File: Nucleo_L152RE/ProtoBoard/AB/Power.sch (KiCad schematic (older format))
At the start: 52 parts, among them J1 EXTPower, P10 GND, P11 GND, P12 GND, P13 GND, P14 GND, P15 GND, P16 GND, P17 GND, P18 GND, P19 3.3Ctl, P20 3.3Ctl, P21 3.3Ctl, P22 3.3V, P23 3.3V, P24 3.3V, P25 5.0V, P26 5.0V, P27 5.0V, P28 Servo, P29 Servo, P30 Servo, P31 Power2, P33 VinPower, P34 ServoPower, P35 Power1, P7 GND, P8 GND, P9 GND, U1 LDS3985

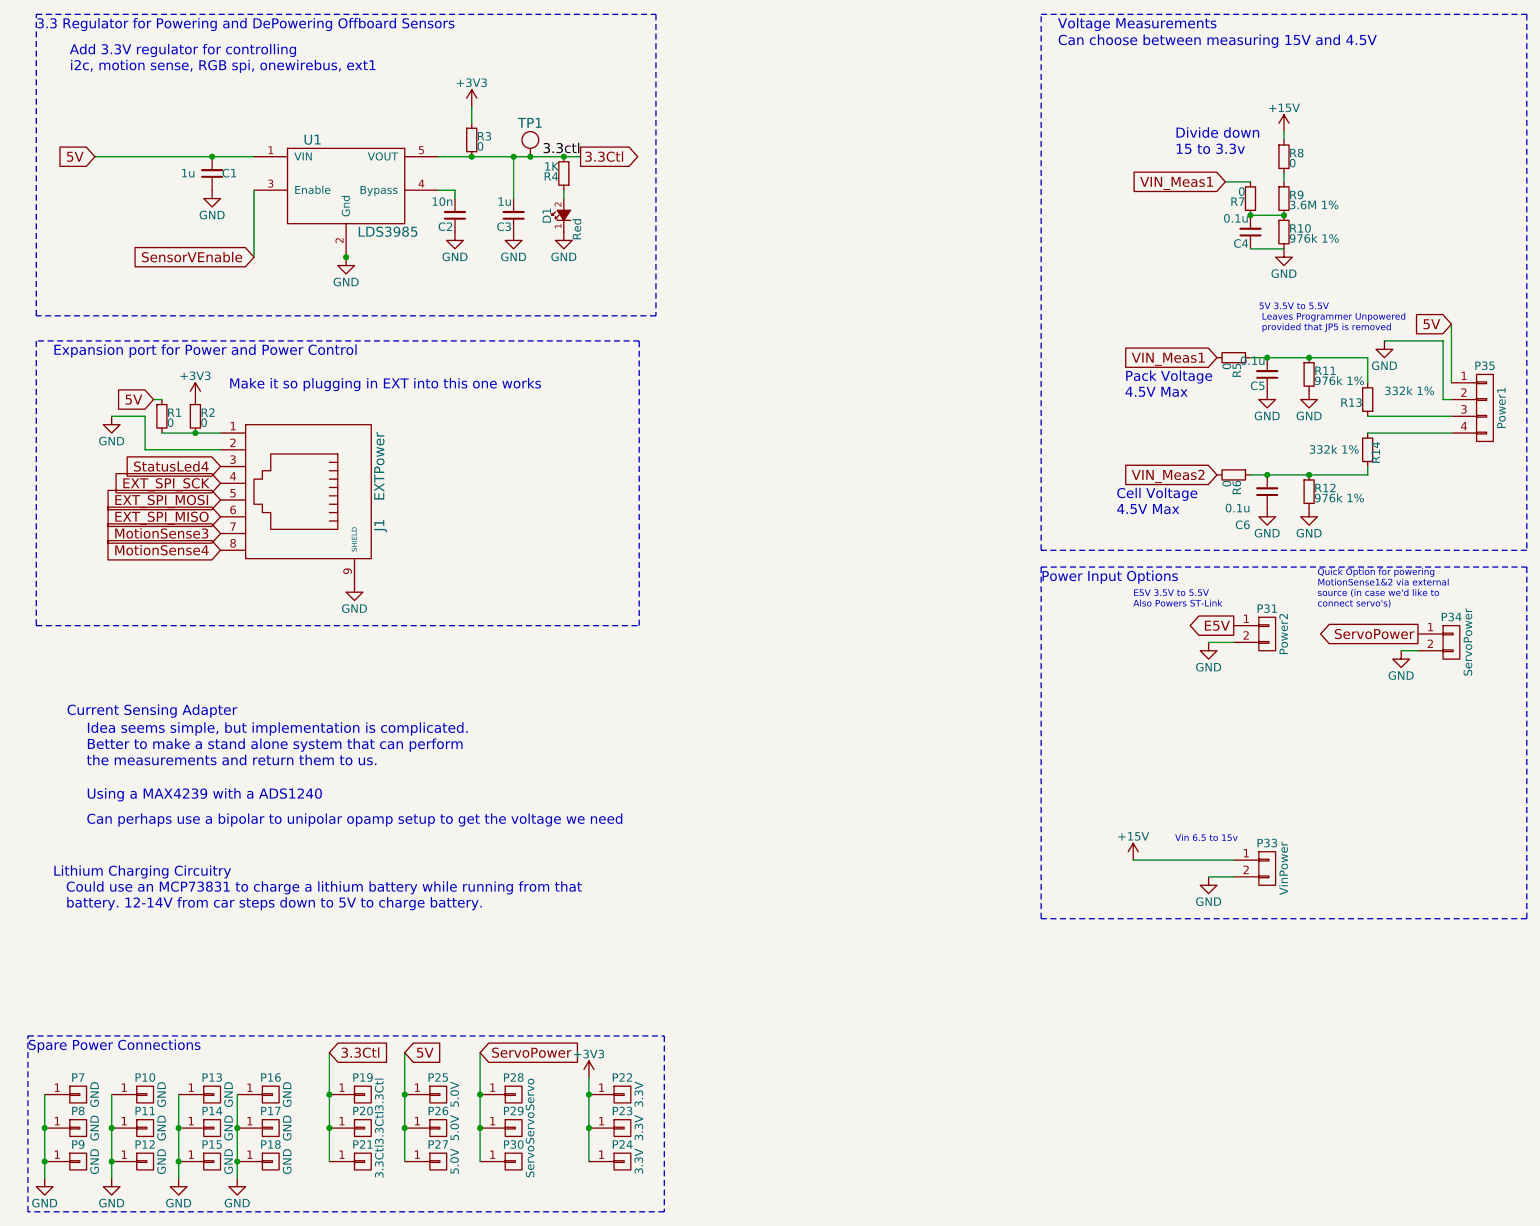
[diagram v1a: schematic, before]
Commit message: Final draft with all traces and artwork in place.
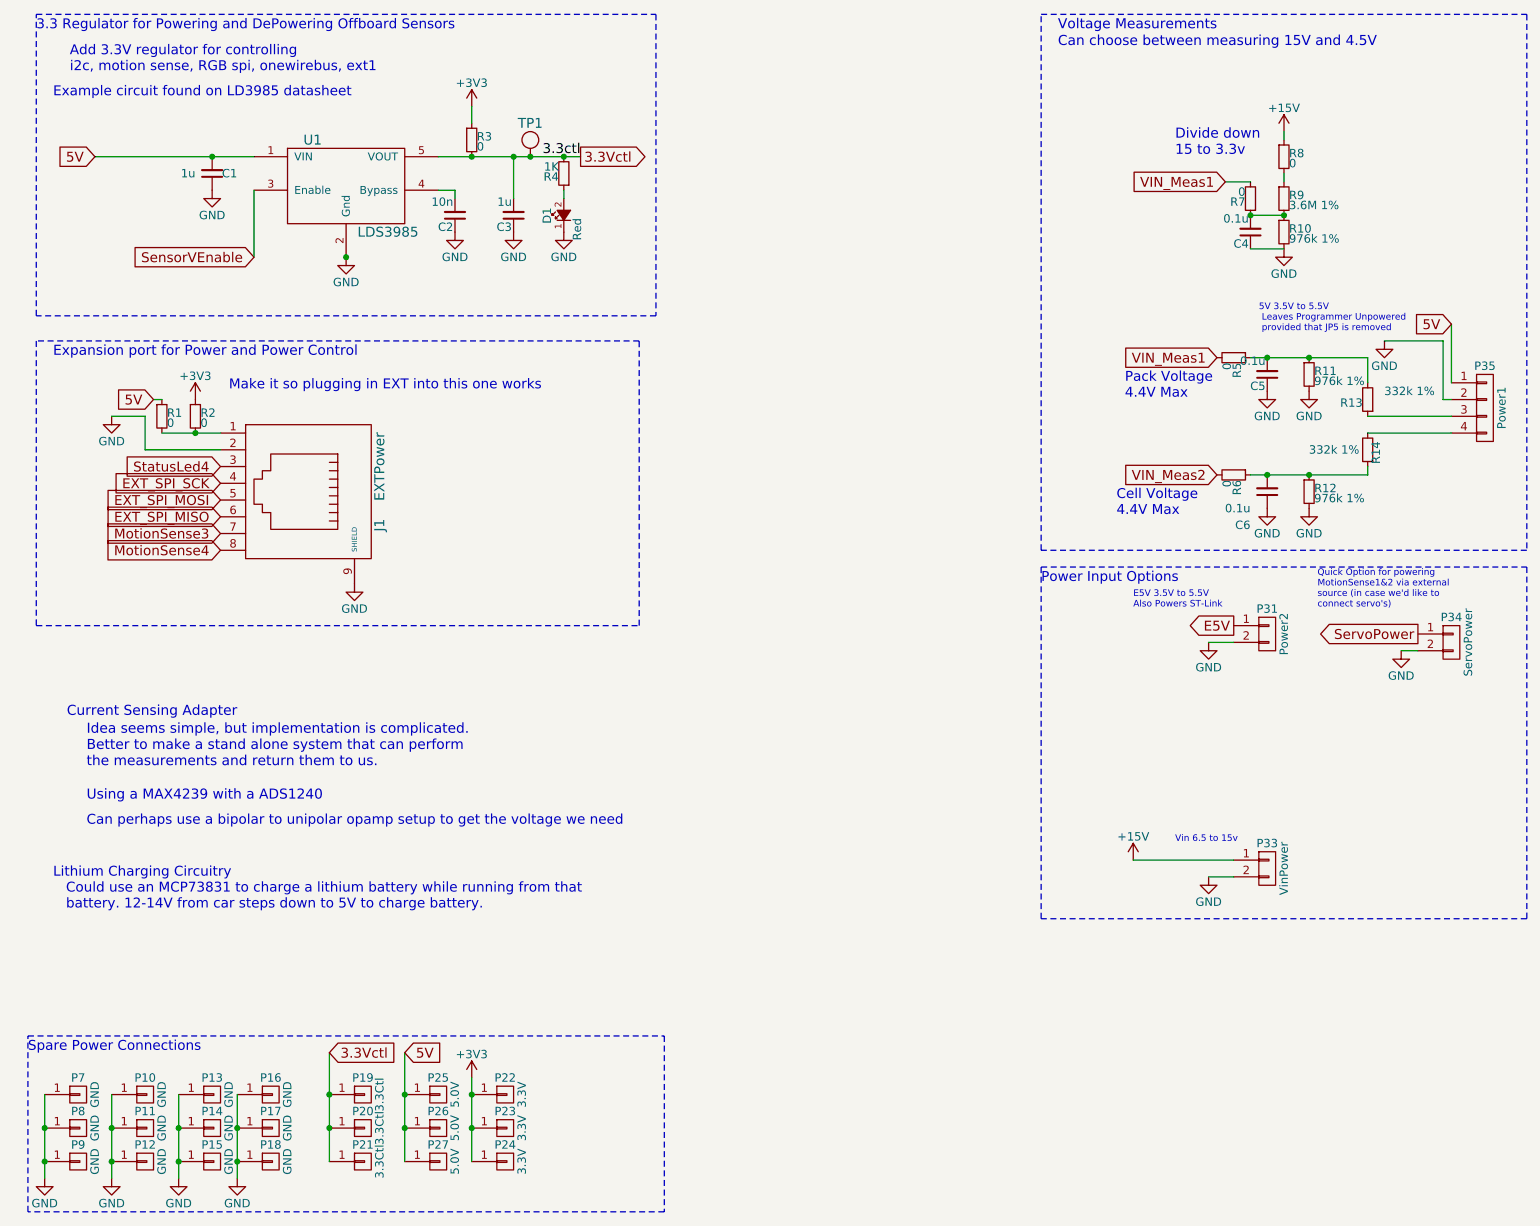
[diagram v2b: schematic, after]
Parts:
- removed P28, P29, P30: Servo, Pin_Headers:Pin_Header_Straight_1x01, symbol CONN_01X01
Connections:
- net 3.3Ctl renamed 3.3Vctl
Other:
- note added: "Cell Voltage\n4.4V Max"
- note added: "Example circuit found on LD3985 datasheet"
- note added: "Pack Voltage\n4.4V Max"
- note removed: "Cell Voltage\n4.5V Max"
- note removed: "Pack Voltage\n4.5V Max"
- moved on the sheet: P22, P23, P24
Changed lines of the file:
@@
 Sheet 2 5
 Title "Expansion Board For STM32 Nucleo-L152RE"
-Date "Saturday, May 23, 2015"
-Rev "AB - Draft"
+Date "Sunday, May 31, 2015"
+Rev "AB - Final Draft"
 Comp "Open Source Hardware"
 Comment1 "MIT License"
@@
 $EndComp
 $Comp
-L GND #PWR04
+L GND #PWR03
 U 1 1 555A6ADF
 P 2550 2100
-F 0 "#PWR04" H 2550 1850 50  0001 C CNN
+F 0 "#PWR03" H 2550 1850 50  0001 C CNN
 F 1 "GND" H 2550 1950 50  0000 C CNN
 F 2 "" H 2550 2100 60  0000 C CNN
@@
 $EndComp
 $Comp
-L GND #PWR05
+L GND #PWR04
 U 1 1 555A6AE5
 P 3200 1950
-F 0 "#PWR05" H 3200 1700 50  0001 C CNN
+F 0 "#PWR04" H 3200 1700 50  0001 C CNN
 F 1 "GND" H 3200 1800 50  0000 C CNN
 F 2 "" H 3200 1950 60  0000 C CNN
@@
 $EndComp
 $Comp
-L GND #PWR06
+L GND #PWR05
 U 1 1 555A6AEB
 P 3550 1950
-F 0 "#PWR06" H 3550 1700 50  0001 C CNN
+F 0 "#PWR05" H 3550 1700 50  0001 C CNN
 F 1 "GND" H 3550 1800 50  0000 C CNN
 F 2 "" H 3550 1950 60  0000 C CNN
@@
 $EndComp
 $Comp
-L GND #PWR07
+L GND #PWR06
 U 1 1 555A6AF1
 P 1750 1700
-F 0 "#PWR07" H 1750 1450 50  0001 C CNN
+F 0 "#PWR06" H 1750 1450 50  0001 C CNN
 F 1 "GND" H 1750 1550 50  0000 C CNN
 F 2 "" H 1750 1700 60  0000 C CNN
@@
 Voltage Measurements\n
 $Comp
-L GND #PWR08
+L GND #PWR07
 U 1 1 555A784D
 P 8150 2050
-F 0 "#PWR08" H 8150 1800 50  0001 C CNN
+F 0 "#PWR07" H 8150 1800 50  0001 C CNN
 F 1 "GND" H 8150 1900 50  0000 C CNN
 F 2 "" H 8150 2050 60  0000 C CNN
@@
 $EndComp
 $Comp
-L GND #PWR09
+L GND #PWR08
 U 1 1 555A7864
 P 7700 4400
-F 0 "#PWR09" H 7700 4150 50  0001 C CNN
+F 0 "#PWR08" H 7700 4150 50  0001 C CNN
 F 1 "GND" H 7700 4250 50  0000 C CNN
 F 2 "" H 7700 4400 60  0000 C CNN
@@
 $EndComp
 $Comp
-L GND #PWR010
+L GND #PWR09
 U 1 1 555A786A
 P 7700 5800
-F 0 "#PWR010" H 7700 5550 50  0001 C CNN
+F 0 "#PWR09" H 7700 5550 50  0001 C CNN
 F 1 "GND" H 7700 5650 50  0000 C CNN
 F 2 "" H 7700 5800 60  0000 C CNN
@@
 $EndComp
 $Comp
-L GND #PWR011
+L GND #PWR010
 U 1 1 555A787C
 P 2600 4050
-F 0 "#PWR011" H 2600 3800 50  0001 C CNN
+F 0 "#PWR010" H 2600 3800 50  0001 C CNN
 F 1 "GND" H 2600 3900 50  0000 C CNN
 F 2 "" H 2600 4050 60  0000 C CNN
@@
 $EndComp
 $Comp
-L GND #PWR012
+L GND #PWR011
 U 1 1 555A7885
 P 1150 3050
-F 0 "#PWR012" H 1150 2800 50  0001 C CNN
+F 0 "#PWR011" H 1150 2800 50  0001 C CNN
 F 1 "GND" H 1150 2900 50  0000 C CNN
 F 2 "" H 1150 3050 60  0000 C CNN
@@
 Expansion port for Power and Power Control\n
 $Comp
-L +15V #PWR013
+L +15V #PWR012
 U 1 1 555A788E
 P 7250 5700
-F 0 "#PWR013" H 7250 5550 50  0001 C CNN
+F 0 "#PWR012" H 7250 5550 50  0001 C CNN
 F 1 "+15V" H 7250 5840 50  0000 C CNN
 F 2 "" H 7250 5700 60  0000 C CNN
@@
 $EndComp
 $Comp
-L +15V #PWR014
+L +15V #PWR013
 U 1 1 555A7894
 P 8150 1350
-F 0 "#PWR014" H 8150 1200 50  0001 C CNN
+F 0 "#PWR013" H 8150 1200 50  0001 C CNN
 F 1 "+15V" H 8150 1490 50  0000 C CNN
 F 2 "" H 8150 1350 60  0000 C CNN
@@
 	1350 3050 1150 3050
 $Comp
-L +3V3 #PWR015
+L +3V3 #PWR014
 U 1 1 555A78D8
 P 1650 2950
-F 0 "#PWR015" H 1650 2800 50  0001 C CNN
+F 0 "#PWR014" H 1650 2800 50  0001 C CNN
 F 1 "+3V3" H 1650 3090 50  0000 C CNN
 F 2 "" H 1650 2950 60  0000 C CNN
@@
 $EndComp
 $Comp
-L GND #PWR016
+L GND #PWR015
 U 1 1 555A7927
 P 8750 2600
-F 0 "#PWR016" H 8750 2350 50  0001 C CNN
+F 0 "#PWR015" H 8750 2350 50  0001 C CNN
 F 1 "GND" H 8750 2450 50  0000 C CNN
 F 2 "" H 8750 2600 60  0000 C CNN
@@
 $EndComp
 Text Notes 7150 3650 0    59   ~ 0
-Cell Voltage\n4.5V Max
+Cell Voltage\n4.4V Max
 Text Notes 7200 2950 0    59   ~ 0
-Pack Voltage\n4.5V Max
+Pack Voltage\n4.4V Max
 Wire Wire Line
 	9150 2500 9150 2850
@@
 $EndComp
 $Comp
-L GND #PWR017
+L GND #PWR016
 U 1 1 555A796E
 P 8300 2900
-F 0 "#PWR017" H 8300 2650 50  0001 C CNN
+F 0 "#PWR016" H 8300 2650 50  0001 C CNN
 F 1 "GND" H 8300 2750 50  0000 C CNN
 F 2 "" H 8300 2900 60  0000 C CNN
@@
 $EndComp
 $Comp
-L GND #PWR018
+L GND #PWR017
 U 1 1 555A7974
 P 8300 3600
-F 0 "#PWR018" H 8300 3350 50  0001 C CNN
+F 0 "#PWR017" H 8300 3350 50  0001 C CNN
 F 1 "GND" H 8300 3450 50  0000 C CNN
 F 2 "" H 8300 3600 60  0000 C CNN
@@
 Connection ~ 8050 3400
 $Comp
-L GND #PWR019
+L GND #PWR018
 U 1 1 555A797E
 P 8050 3600
-F 0 "#PWR019" H 8050 3350 50  0001 C CNN
+F 0 "#PWR018" H 8050 3350 50  0001 C CNN
 F 1 "GND" H 8050 3450 50  0000 C CNN
 F 2 "" H 8050 3600 60  0000 C CNN
@@
 $EndComp
 $Comp
-L GND #PWR020
+L GND #PWR019
 U 1 1 555A7984
 P 8050 2900
-F 0 "#PWR020" H 8050 2650 50  0001 C CNN
+F 0 "#PWR019" H 8050 2650 50  0001 C CNN
 F 1 "GND" H 8050 2750 50  0000 C CNN
 F 2 "" H 8050 2900 60  0000 C CNN
@@
 SensorVEnable
 Text GLabel 3950 1500 2    59   Output ~ 0
-3.3Ctl
+3.3Vctl
 Connection ~ 1650 3150
 $Comp
@@
 	3300 1300 3300 1200
 $Comp
-L +3V3 #PWR021
+L +3V3 #PWR020
 U 1 1 555CFD1C
 P 3300 1200
-F 0 "#PWR021" H 3300 1050 50  0001 C CNN
+F 0 "#PWR020" H 3300 1050 50  0001 C CNN
 F 1 "+3V3" H 3300 1340 50  0000 C CNN
 F 2 "" H 3300 1200 60  0000 C CNN
@@
 	4300 2600 700  2600
 $Comp
-L GND #PWR022
+L GND #PWR021
 U 1 1 555BF489
 P 8850 4450
-F 0 "#PWR022" H 8850 4200 50  0001 C CNN
+F 0 "#PWR021" H 8850 4200 50  0001 C CNN
 F 1 "GND" H 8850 4300 50  0000 C CNN
 F 2 "" H 8850 4450 60  0000 C CNN
@@
 	3850 1750 3850 1700
 $Comp
-L GND #PWR023
+L GND #PWR022
 U 1 1 55612181
 P 3850 1950
-F 0 "#PWR023" H 3850 1700 50  0001 C CNN
+F 0 "#PWR022" H 3850 1700 50  0001 C CNN
 F 1 "GND" H 3850 1800 50  0000 C CNN
 F 2 "" H 3850 1950 60  0000 C CNN
@@
 $EndComp
 $Comp
-L GND #PWR024
+L GND #PWR023
 U 1 1 5561927C
 P 750 7600
-F 0 "#PWR024" H 750 7350 50  0001 C CNN
+F 0 "#PWR023" H 750 7350 50  0001 C CNN
 F 1 "GND" H 750 7450 50  0000 C CNN
 F 2 "" H 750 7600 60  0000 C CNN
@@
 $EndComp
 $Comp
-L GND #PWR025
+L GND #PWR024
 U 1 1 55619337
 P 1550 7600
-F 0 "#PWR025" H 1550 7350 50  0001 C CNN
+F 0 "#PWR024" H 1550 7350 50  0001 C CNN
 F 1 "GND" H 1550 7450 50  0000 C CNN
 F 2 "" H 1550 7600 60  0000 C CNN
@@
 $EndComp
 $Comp
-L GND #PWR026
+L GND #PWR025
 U 1 1 5561939A
 P 1900 7600
-F 0 "#PWR026" H 1900 7350 50  0001 C CNN
+F 0 "#PWR025" H 1900 7350 50  0001 C CNN
 F 1 "GND" H 1900 7450 50  0000 C CNN
 F 2 "" H 1900 7600 60  0000 C CNN
@@
 	1    0    0    -1
 $EndComp
-$Comp
-L CONN_01X01 P28
-U 1 1 556194D9
-P 3550 7100
-F 0 "P28" H 3550 7200 50  0000 C CNN
-F 1 "Servo" V 3650 7100 50  0000 C CNN
-F 2 "Pin_Headers:Pin_Header_Straight_1x01" H 3550 7100 60  0001 C CNN
-F 3 "" H 3550 7100 60  0000 C CNN
-	1    3550 7100
-	1    0    0    -1
-$EndComp
-$Comp
-L CONN_01X01 P29
-U 1 1 55619647
-P 3550 7300
-F 0 "P29" H 3550 7400 50  0000 C CNN
-F 1 "Servo" V 3650 7300 50  0000 C CNN
-F 2 "Pin_Headers:Pin_Header_Straight_1x01" H 3550 7300 60  0001 C CNN
-F 3 "" H 3550 7300 60  0000 C CNN
-	1    3550 7300
-	1    0    0    -1
-$EndComp
-$Comp
-L CONN_01X01 P30
-U 1 1 556196B9
-P 3550 7500
-F 0 "P30" H 3550 7600 50  0000 C CNN
-F 1 "Servo" V 3650 7500 50  0000 C CNN
-F 2 "Pin_Headers:Pin_Header_Straight_1x01" H 3550 7500 60  0001 C CNN
-F 3 "" H 3550 7500 60  0000 C CNN
-	1    3550 7500
-	1    0    0    -1
-$EndComp
-Text GLabel 3350 6850 2    59   Input ~ 0
-ServoPower
 Text GLabel 2900 6850 2    59   Input ~ 0
 5V
 $Comp
-L +3V3 #PWR027
+L +3V3 #PWR026
 U 1 1 55619913
-P 4000 7000
-F 0 "#PWR027" H 4000 6850 50  0001 C CNN
-F 1 "+3V3" H 4000 7140 50  0000 C CNN
-F 2 "" H 4000 7000 60  0000 C CNN
-F 3 "" H 4000 7000 60  0000 C CNN
-	1    4000 7000
+P 3300 7000
+F 0 "#PWR026" H 3300 6850 50  0001 C CNN
+F 1 "+3V3" H 3300 7140 50  0000 C CNN
+F 2 "" H 3300 7000 60  0000 C CNN
+F 3 "" H 3300 7000 60  0000 C CNN
+	1    3300 7000
 	1    0    0    -1
 $EndComp
 Text GLabel 2450 6850 2    59   Input ~ 0
-3.3Ctl
+3.3Vctl
 $Comp
 L CONN_01X01 P22
 U 1 1 55619BE1
-P 4200 7100
-F 0 "P22" H 4200 7200 50  0000 C CNN
-F 1 "3.3V" V 4300 7100 50  0000 C CNN
-F 2 "Pin_Headers:Pin_Header_Straight_1x01" H 4200 7100 60  0001 C CNN
-F 3 "" H 4200 7100 60  0000 C CNN
-	1    4200 7100
+P 3500 7100
+F 0 "P22" H 3500 7200 50  0000 C CNN
+F 1 "3.3V" V 3600 7100 50  0000 C CNN
+F 2 "Pin_Headers:Pin_Header_Straight_1x01" H 3500 7100 60  0001 C CNN
+F 3 "" H 3500 7100 60  0000 C CNN
+	1    3500 7100
 	1    0    0    -1
 $EndComp
@@
 L CONN_01X01 P23
 U 1 1 55619CCF
-P 4200 7300
-F 0 "P23" H 4200 7400 50  0000 C CNN
-F 1 "3.3V" V 4300 7300 50  0000 C CNN
-F 2 "Pin_Headers:Pin_Header_Straight_1x01" H 4200 7300 60  0001 C CNN
-F 3 "" H 4200 7300 60  0000 C CNN
-	1    4200 7300
+P 3500 7300
+F 0 "P23" H 3500 7400 50  0000 C CNN
+F 1 "3.3V" V 3600 7300 50  0000 C CNN
+F 2 "Pin_Headers:Pin_Header_Straight_1x01" H 3500 7300 60  0001 C CNN
+F 3 "" H 3500 7300 60  0000 C CNN
+	1    3500 7300
 	1    0    0    -1
 $EndComp
@@
 L CONN_01X01 P24
 U 1 1 55619D47
-P 4200 7500
-F 0 "P24" H 4200 7600 50  0000 C CNN
-F 1 "3.3V" V 4300 7500 50  0000 C CNN
-F 2 "Pin_Headers:Pin_Header_Straight_1x01" H 4200 7500 60  0001 C CNN
-F 3 "" H 4200 7500 60  0000 C CNN
-	1    4200 7500
-	1    0    0    -1
-$EndComp
-Wire Wire Line
-	4000 7000 4000 7500
-Connection ~ 4000 7100
-Connection ~ 4000 7300
+P 3500 7500
+F 0 "P24" H 3500 7600 50  0000 C CNN
+F 1 "3.3V" V 3600 7500 50  0000 C CNN
+F 2 "Pin_Headers:Pin_Header_Straight_1x01" H 3500 7500 60  0001 C CNN
+F 3 "" H 3500 7500 60  0000 C CNN
+	1    3500 7500
+	1    0    0    -1
+$EndComp
+Wire Wire Line
+	3300 7000 3300 7500
+Connection ~ 3300 7100
+Connection ~ 3300 7300
 Wire Wire Line
 	2450 6850 2450 7500
@@
 Connection ~ 2900 7100
 Connection ~ 2900 7300
-Wire Wire Line
-	3350 6850 3350 7500
-Connection ~ 3350 7100
-Connection ~ 3350 7300
 Wire Wire Line
 	1900 7100 1900 7600
@@
 $EndComp
 $Comp
-L GND #PWR028
+L GND #PWR027
 U 1 1 5561B03D
 P 1150 7600
-F 0 "#PWR028" H 1150 7350 50  0001 C CNN
+F 0 "#PWR027" H 1150 7350 50  0001 C CNN
 F 1 "GND" H 1150 7450 50  0000 C CNN
 F 2 "" H 1150 7600 60  0000 C CNN
@@
 Wire Notes Line
 	6700 3850 6700 650
+Text Notes 800  1150 0    59   ~ 0
+Example circuit found on LD3985 datasheet
 $EndSCHEMATC
